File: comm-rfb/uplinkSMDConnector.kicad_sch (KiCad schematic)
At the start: 2 parts

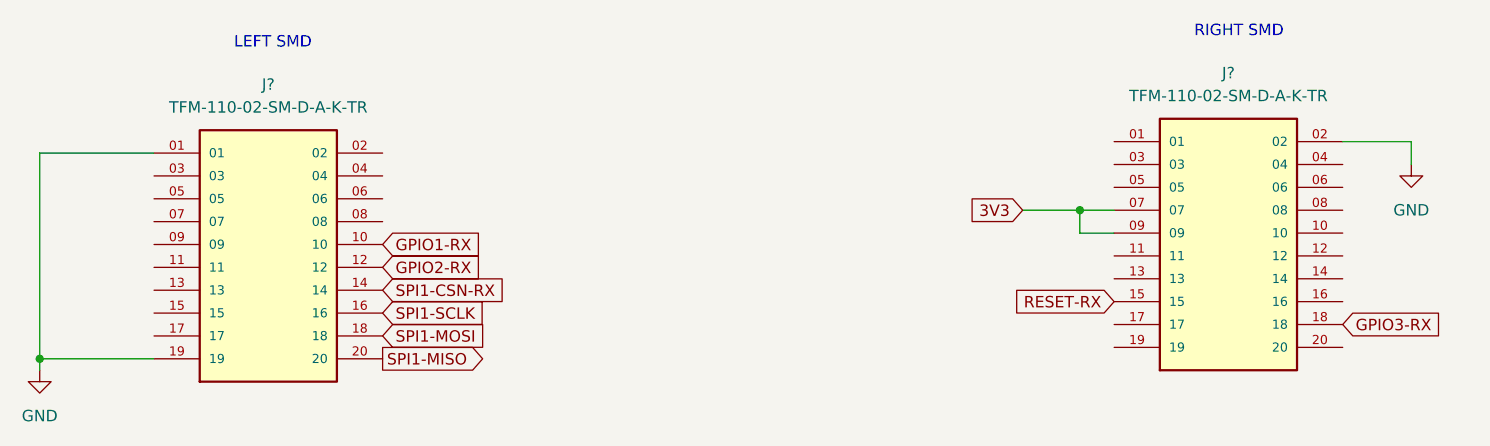
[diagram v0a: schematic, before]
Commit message: added mcu connections
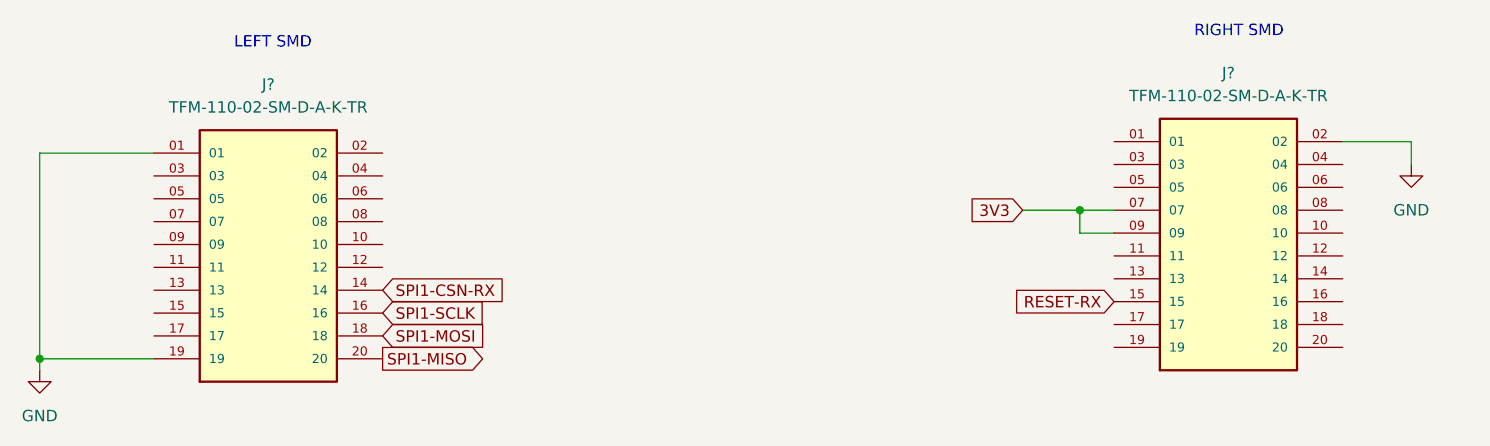
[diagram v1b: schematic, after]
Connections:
- net GPIO1-RX: no longer names the net of J?.10
- net GPIO2-RX: no longer names the net of J?.12
- net GPIO3-RX: no longer names the net of J?.18
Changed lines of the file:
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@@
     (effects (font (size 1.27 1.27)) (justify left bottom))
-  )
-  (global_label "GPIO2-RX" (shape input) (at 110.49 87.63 0) (fields_autoplaced)
-    (effects (font (size 1.27 1.27)) (justify left))
-    (property "Intersheet References" "${INTERSHEET_REFS}" (id 0) (at 122.6398 87.5506 0)
-      (effects (font (size 1.27 1.27)) (justify left) hide)
-    )
   )
   (global_label "SPI1-CSN-RX" (shape input) (at 110.49 90.17 0) (fields_autoplaced)
@@
       (effects (font (size 1.27 1.27)) (justify left) hide)
     )
-  )
-  (global_label "GPIO3-RX" (shape input) (at 217.17 93.98 0) (fields_autoplaced)
-    (effects (font (size 1.27 1.27)) (justify left))
-    (property "Intersheet References" "${INTERSHEET_REFS}" (id 0) (at 229.3198 93.9006 0)
-      (effects (font (size 1.27 1.27)) (justify left) hide)
-    )
-  )
-  (global_label "GPIO1-RX" (shape input) (at 110.49 85.09 0) (fields_autoplaced)
-    (effects (font (size 1.27 1.27)) (justify left))
-    (property "Intersheet References" "${INTERSHEET_REFS}" (id 0) (at 122.6398 85.0106 0)
-      (effects (font (size 1.27 1.27)) (justify left) hide)
-    )

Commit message: comm-rfb: reformat main schematic page
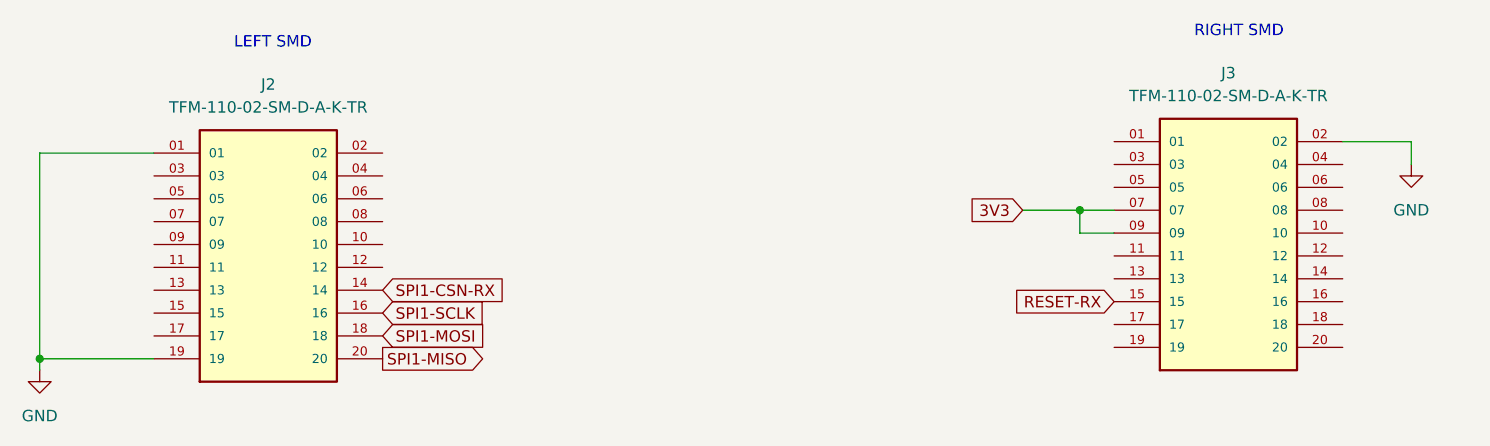
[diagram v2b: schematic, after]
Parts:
- gave numbers to parts that had none: 2
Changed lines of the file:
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@@
   (symbol (lib_id "TFM-110-02-SM-D-A-K-TR:TFM-110-02-SM-D-A-K-TR") (at 97.79 87.63 0) (unit 1)
     (in_bom yes) (on_board yes) (fields_autoplaced)
-    (property "Reference" "J?" (id 0) (at 97.79 67.31 0))
+    (property "Reference" "J2" (id 0) (at 97.79 67.31 0))
     (property "Value" "TFM-110-02-SM-D-A-K-TR" (id 1) (at 97.79 69.85 0))
     (property "Footprint" "SAMTEC_TFM-110-02-SM-D-A-K-TR" (id 2) (at 97.79 87.63 0)
@@
   (symbol (lib_id "power:GND") (at 224.79 76.2 0) (unit 1)
     (in_bom yes) (on_board yes) (fields_autoplaced)
-    (property "Reference" "#PWR?" (id 0) (at 224.79 82.55 0)
+    (property "Reference" "#PWR02" (id 0) (at 224.79 82.55 0)
       (effects (font (size 1.27 1.27)) hide)
     )
@@
   (symbol (lib_id "power:GND") (at 72.39 99.06 0) (unit 1)
     (in_bom yes) (on_board yes) (fields_autoplaced)
-    (property "Reference" "#PWR?" (id 0) (at 72.39 105.41 0)
+    (property "Reference" "#PWR01" (id 0) (at 72.39 105.41 0)
       (effects (font (size 1.27 1.27)) hide)
     )
@@
   (symbol (lib_id "TFM-110-02-SM-D-A-K-TR:TFM-110-02-SM-D-A-K-TR") (at 204.47 86.36 0) (unit 1)
     (in_bom yes) (on_board yes) (fields_autoplaced)
-    (property "Reference" "J?" (id 0) (at 204.47 66.04 0))
+    (property "Reference" "J3" (id 0) (at 204.47 66.04 0))
     (property "Value" "TFM-110-02-SM-D-A-K-TR" (id 1) (at 204.47 68.58 0))
     (property "Footprint" "SAMTEC_TFM-110-02-SM-D-A-K-TR" (id 2) (at 204.47 86.36 0)
